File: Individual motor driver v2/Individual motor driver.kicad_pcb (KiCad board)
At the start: 2 copper layers, 100 x 100 mm, 39 parts, among them P1 CONN_01X06, P2 CONN_01X01, P3 CONN_01X02, P4 CONN_01X06, P5 CONN_01X02, P6 CONN_01X02, P7 CONN_01X01, P9 CONN_01X02, Q1 PN2222A, Q2 PN2222A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

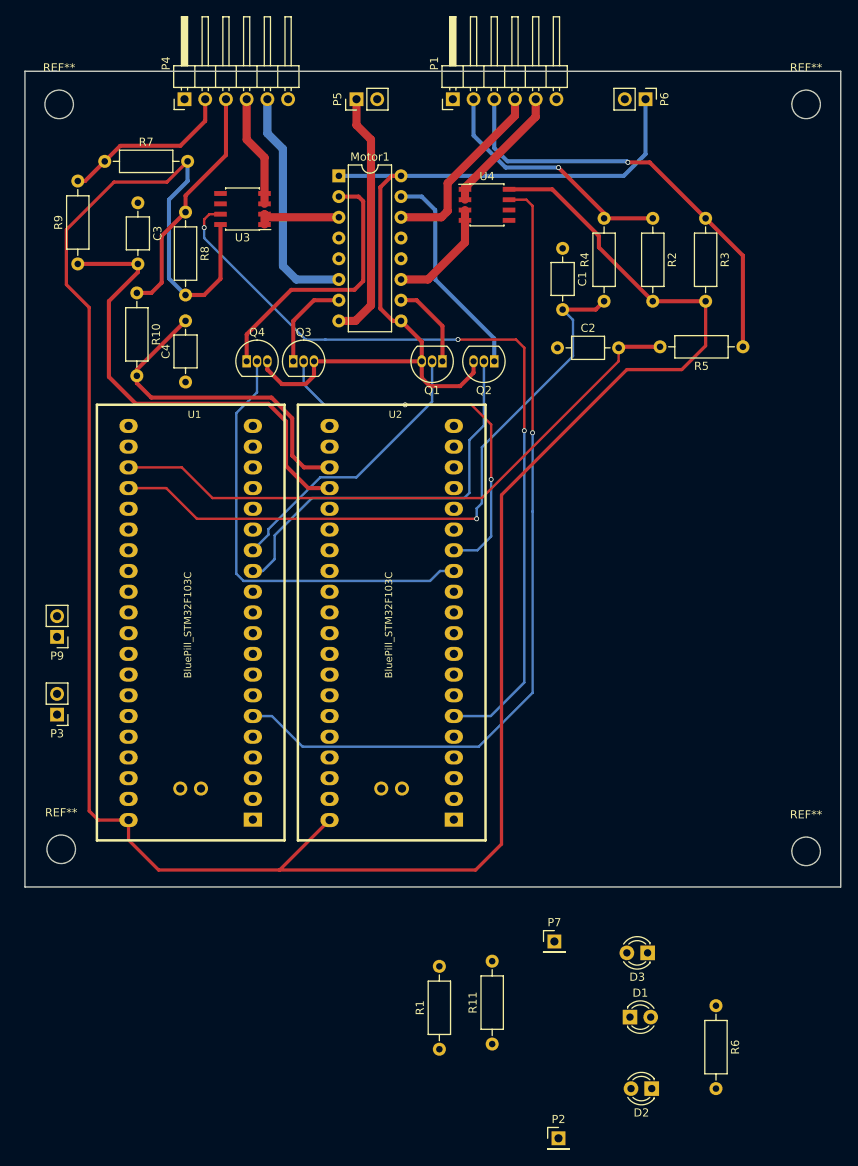
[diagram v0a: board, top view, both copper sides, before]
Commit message: Continued routing on board
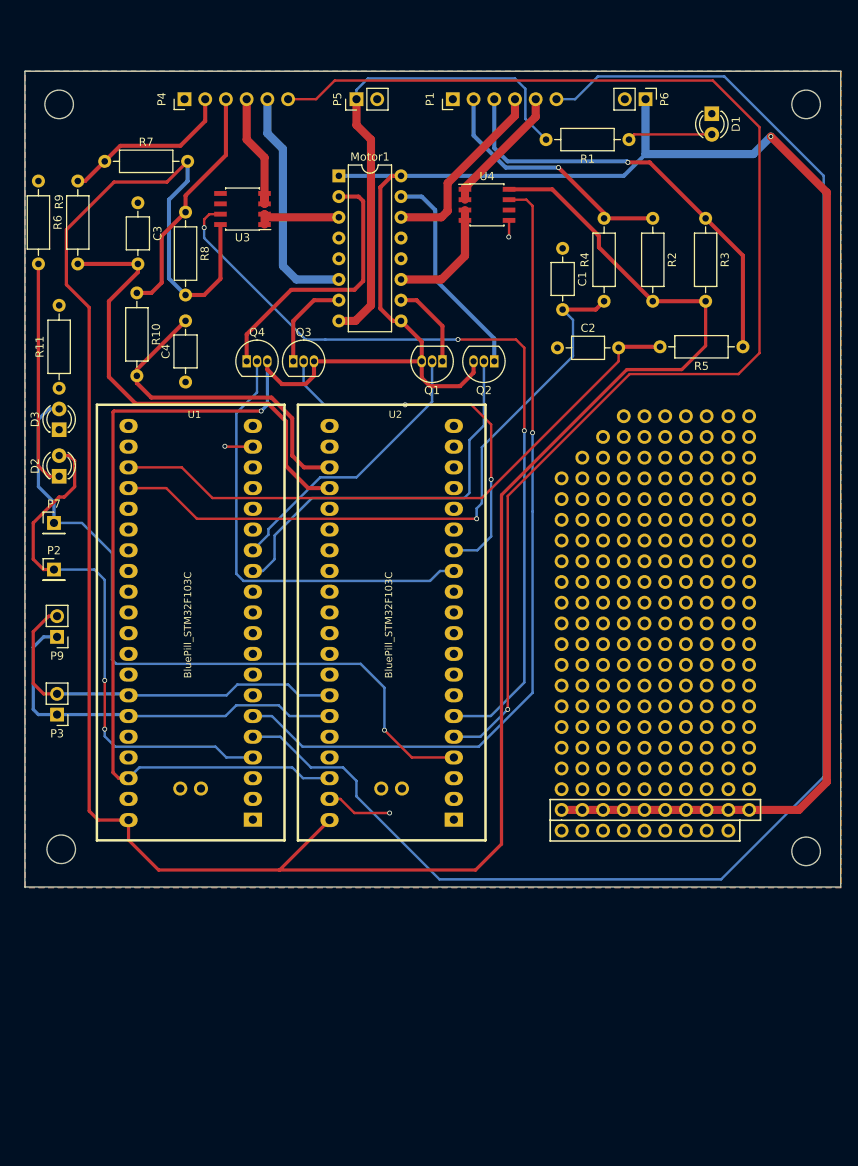
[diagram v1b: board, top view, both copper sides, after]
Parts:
- added REF**: Pin_Header_Straight_2x21_Pitch2.54mm, Pin_Headers:Pin_Header_Straight_2x21_Pitch2.54mm, F.Cu at (148.0, 80.3)
- added REF**: Pin_Header_Straight_2x21_Pitch2.54mm, Pin_Headers:Pin_Header_Straight_2x21_Pitch2.54mm, F.Cu at (168.4, 80.3)
- added REF**: Pin_Header_Straight_2x21_Pitch2.54mm, Pin_Headers:Pin_Header_Straight_2x21_Pitch2.54mm, F.Cu at (153.0, 80.3)
- added REF**: Pin_Header_Straight_2x21_Pitch2.54mm, Pin_Headers:Pin_Header_Straight_2x21_Pitch2.54mm, F.Cu at (163.2, 80.3)
- added REF**: Pin_Header_Straight_2x21_Pitch2.54mm, Pin_Headers:Pin_Header_Straight_2x21_Pitch2.54mm, F.Cu at (158.1, 80.3)
- moved R6 130.8 mm to (83.8, 51.4)
- moved R1 113.9 mm to (156.2, 46.4), turned to 180 degrees
- moved D1 111.2 mm to (166.4, 43.2), turned to 270 degrees
- moved D2 104.5 mm to (86.4, 87.6), turned to 90 degrees
- moved D3 96.5 mm to (86.4, 81.9), turned to 90 degrees
- moved R11 96.3 mm to (86.4, 76.8)
- moved P2 93.2 mm to (85.7, 99.1)
- moved P7 80.0 mm to (85.7, 93.3)
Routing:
- net 5V: track 106.3 -> 335.2 mm, vias 0 -> 2
- net Limit2: track 0.00 -> 196.2 mm
- net Limit1: track 0.00 -> 161.1 mm, vias 0 -> 1
- net Stall_1: track 0.00 -> 88.2 mm, vias 0 -> 1
- net Stall_2: track 0.00 -> 64.9 mm, vias 0 -> 2
- net SDA: track 0.00 -> 48.8 mm
- net SCL: track 0.00 -> 48.1 mm
- net VCC: track 30.7 -> 61.0 mm
- net Net-(D2-Pad1): track 0.00 -> 27.8 mm
- net GND: track 0.00 -> 13.6 mm, vias 0 -> 3
- net Net-(D1-Pad2): track 0.00 -> 10.4 mm
- net M2:O2: track 13.7 -> 19.0 mm
- net M1:1: track 13.7 -> 15.0 mm
- added copper zone on B.Cu, net GND
- added copper zone on F.Cu, net GND

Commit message: Finished routing and added silkscreen
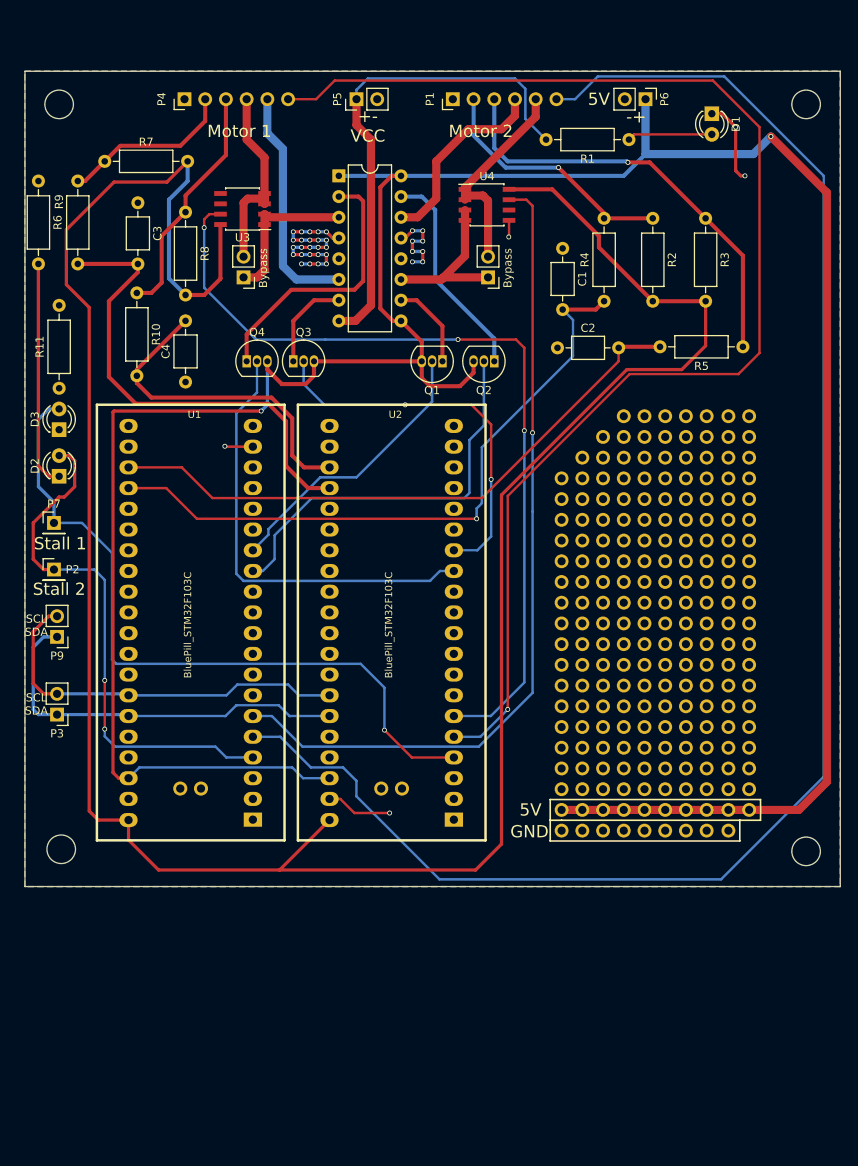
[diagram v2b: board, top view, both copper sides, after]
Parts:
- added Bypass: PinHeader_1x02_P2.54mm_Vertical, Connector_PinHeader_2.54mm:PinHeader_1x02_P2.54mm_Vertical, F.Cu at (109.0, 63.2)
- added Bypass: PinHeader_1x02_P2.54mm_Vertical, Connector_PinHeader_2.54mm:PinHeader_1x02_P2.54mm_Vertical, F.Cu at (138.9, 63.2)
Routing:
- net GND: track 13.6 -> 59.7 mm, vias 3 -> 37
- net M2:2: track 15.9 -> 25.9 mm
- net M1:1: track 15.0 -> 24.4 mm
- net M1:O1: track 10.5 -> 19.0 mm
- net M2:O2: track 19.0 -> 24.8 mm
- net M1:Current: track 100.7 -> 104.3 mm
- net M2:1: track 23.2 -> 23.8 mm
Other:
- board size 100 x 100 mm -> 99.9 x 99.9 mm
- board text added: "+- VCC"
- board text added: "-+"
- board text added: "5V"
- board text added: "GND"
- board text added: "Motor 1"
- board text added: "Motor 2"
- board text added: "Motor driver V2 By Ethan https://github.com/ethanleep/robotic-arm"
- board text added: "SCL SDA"
- board text added: "Stall 1"
- board text added: "Stall 2"

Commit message: Updated V2 files
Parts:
- moved REF** 0.40 mm to (86.5, 133.7)
- moved REF** 0.18 mm to (86.5, 42.2)
- moved REF** 0.18 mm to (177.8, 42.2)
- moved REF** 0.18 mm to (177.8, 133.7)
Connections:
- REF** pad 37: (no net) -> 3.3v (x5)
- REF** pad 38: (no net) -> 3.3v (x5)
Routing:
- net 3.3v: track 297.1 -> 329.9 mm
- net GND: track 59.7 -> 78.5 mm, vias 37 -> 46
- net Net-(D3-Pad1): track 0.00 -> 16.6 mm
- net VCC: track 61.0 -> 61.8 mm
- net 5V: track 335.2 -> 334.5 mm
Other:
- outline, holes or cut-outs redrawn
- board text added: "3.3V"
